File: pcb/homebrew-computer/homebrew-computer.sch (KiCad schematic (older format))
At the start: 4 parts

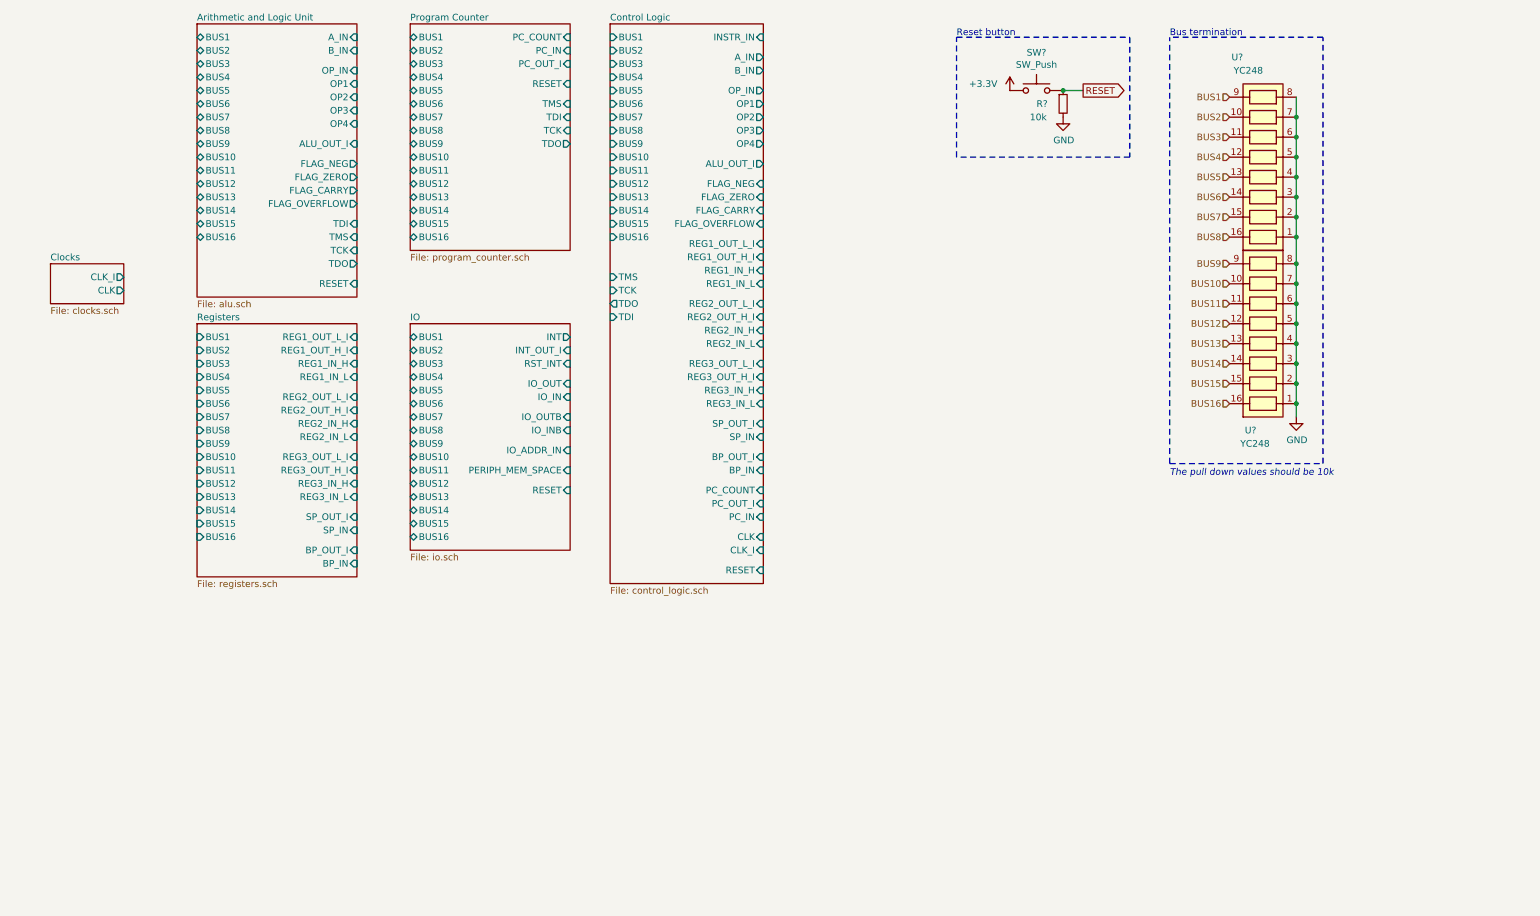
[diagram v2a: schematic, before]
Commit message: Connect signals between modules
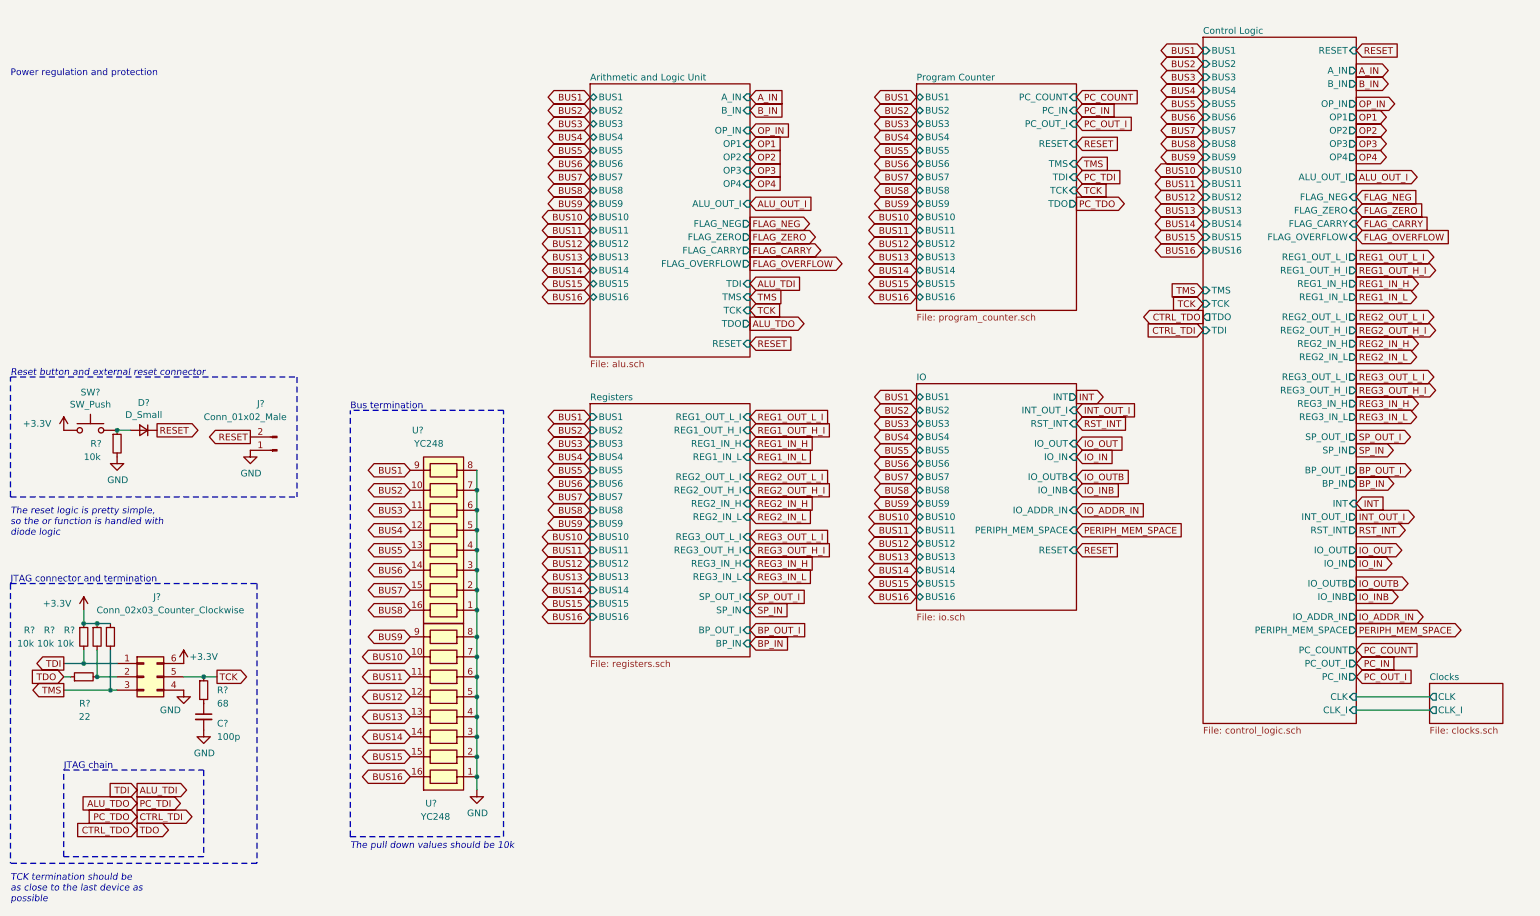
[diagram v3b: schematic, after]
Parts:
- added C?: 100p, symbol Device:C_Small
- added D?: D_Small, symbol Device:D_Small
- added J?: Conn_02x03_Counter_Clockwise, symbol Connector_Generic:Conn_02x03_Counter_Clockwise
- added J?: Conn_01x02_Male, symbol Connector:Conn_01x02_Male
- added R? (x3): 10k, symbol Device:R_Small
- added R?: 68, symbol Device:R_Small
- added R?: 22, symbol Device:R_Small
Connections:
- net +3V3: now also J?.6 (Pin_6), R?.1, R?.1, R?.1
- net GND: now also C?.2, J?.1 (Pin_1), J?.4 (Pin_4)
- net RESET: now also D?.1 (K), J?.2 (Pin_2); no longer R?.1, SW?.2
- new net: J?.2 (Pin_2), R?.2, R?.2
- new net: C?.1, R?.2
- new net: D?.2 (A), R?.1, SW?.2
- new net ALU_TDI: J?.1 (Pin_1), R?.2
- new net CTRL_TDO: R?.1
- new net TCK: J?.5 (Pin_5), R?.1
- new net TMS: J?.3 (Pin_3), R?.2
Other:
- note added: "JTAG chain"
- note added: "JTAG connector and termination"
- note added: "Power regulation and protection"
- note added: "Reset button and external reset connector"
- note added: "TCK termination should be \nas close to the last device as\npossible"
- note added: "The reset logic is pretty simple, \nso the or function is handled with\ndiode logic"
- note removed: "Reset button"
- moved on the sheet: R?, SW?, U?

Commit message: Start changing global labels with local labels
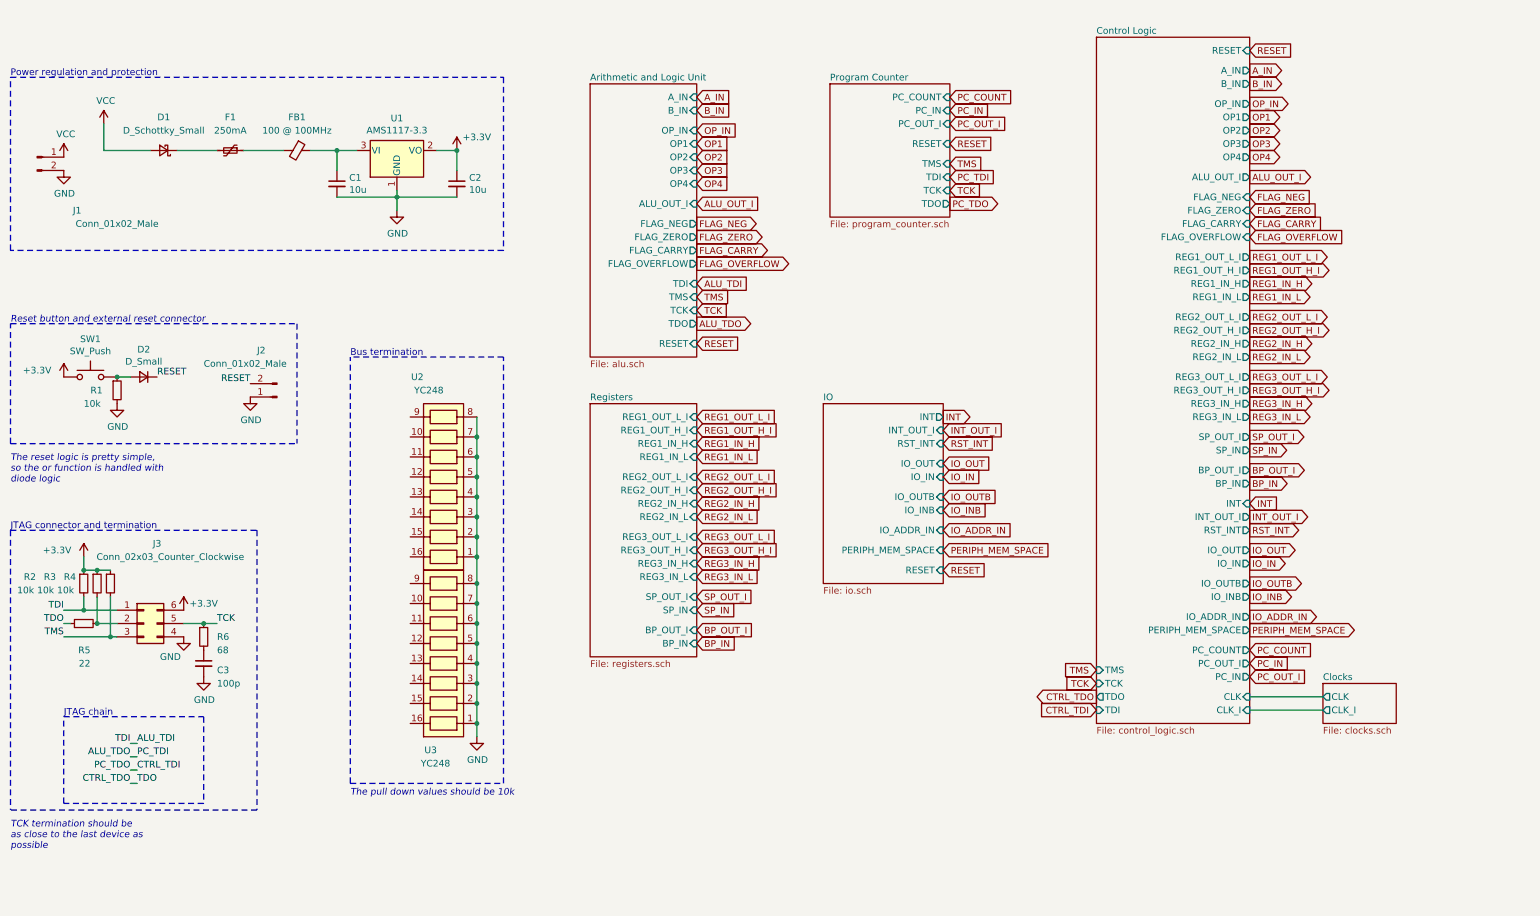
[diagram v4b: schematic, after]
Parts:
- added C1, C2: 10u, symbol Device:C_Small
- added D1: D_Schottky_Small, symbol Device:D_Schottky_Small
- added F1: 250mA, symbol Device:Polyfuse_Small
- added FB1: 100 @ 100MHz, symbol Device:Ferrite_Bead_Small
- added J1: Conn_01x02_Male, symbol Connector:Conn_01x02_Male
- added U1: AMS1117-3.3, Package_TO_SOT_SMD:SOT-223-3_TabPin2, symbol Regulator_Linear:AMS1117-3.3
- gave numbers to parts that had none: 13
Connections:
- net +3V3: now also C2.1, U1.2 (VO)
- net GND: now also C1.2, C2.2, J1.2 (Pin_2), U1.1 (GND)
- net BUS1: no longer names the net of U2.9
- net BUS10: no longer names the net of U3.10
- net BUS11: no longer names the net of U3.11
- net BUS12: no longer names the net of U3.12
- net BUS13: no longer names the net of U3.13
- net BUS14: no longer names the net of U3.14
- net BUS15: no longer names the net of U3.15
- net BUS16: no longer names the net of U3.16
- net BUS2: no longer names the net of U2.10
- net BUS3: no longer names the net of U2.11
- net BUS4: no longer names the net of U2.12
- net BUS5: no longer names the net of U2.13
- net BUS6: no longer names the net of U2.14
- net BUS7: no longer names the net of U2.15
- net BUS8: no longer names the net of U2.16
- net BUS9: no longer names the net of U3.9
- new net: F1.1, FB1.2
- new net: D1.1 (K), F1.2
- new net: C1.1, FB1.1, U1.3 (VI)
- new net VCC: D1.2 (A), J1.1 (Pin_1)
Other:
- moved on the sheet: C3, D2, J2, J3, R1, R2, R3, R4, R5, R6, SW1, U2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

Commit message: Start working on the pcb layout
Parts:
- C1, C2: footprint (none) -> Capacitor_SMD:C_0603_1608Metric
- C3: footprint (none) -> Capacitor_SMD:C_0402_1005Metric_Pad0.74x0.62mm_HandSolder
- D1, D2: footprint (none) -> Diode_SMD:D_0603_1608Metric
- F1: footprint (none) -> Fuse:Fuse_1206_3216Metric_Pad1.42x1.75mm_HandSolder
- FB1, R1, R2, R3, R4, R5, R6: footprint (none) -> Resistor_SMD:R_0603_1608Metric
- J1, J2: footprint (none) -> Connector_Molex:Molex_PicoBlade_53048-0210_1x02_P1.25mm_Horizontal
- J3: footprint (none) -> Connector_PinHeader_2.54mm:PinHeader_2x03_P2.54mm_Vertical
- SW1: footprint (none) -> Button_Switch_SMD:Panasonic_EVQPUL_EVQPUC
- U2, U3: footprint (none) -> Resistor_SMD:YC248
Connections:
- net BUS10: now reaches U3.10
- net BUS11: now reaches U3.11
- net BUS12: now reaches U3.12
- net BUS13: now reaches U3.13
- net BUS14: now reaches U3.14
- net BUS15: now reaches U3.15
- net BUS16: now reaches U3.16
- net BUS9: now reaches U3.9
- net BUS2: now reaches U2.10
- net BUS3: now reaches U2.11
- net BUS4: now reaches U2.12
- net BUS5: now reaches U2.13
- net BUS6: now reaches U2.14
- net BUS7: now reaches U2.15
- net BUS8: now reaches U2.16
- net BUS1: now reaches U2.9
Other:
- moved on the sheet: J1

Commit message: Keep working on the layout
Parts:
- J1, J2: footprint Connector_Molex:Molex_PicoBlade_53048-0210_1x02_P1.25mm_Horizontal -> Connector_Molex:Molex_Pico-Clasp_202396-0207_1x02-1MP_P1.00mm_Horizontal
- J3: footprint Connector_PinHeader_2.54mm:PinHeader_2x03_P2.54mm_Vertical -> Connector_Molex:Molex_Pico-Clasp_202396-0607_1x06-1MP_P1.00mm_Horizontal
- R1, R2, R3, R4, R5, R6: footprint Resistor_SMD:R_0603_1608Metric -> Resistor_SMD:R_0402_1005Metric_Pad0.72x0.64mm_HandSolder
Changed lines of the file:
@@
 F 0 "R1" H 1450 3600 50  0000 L CNN
 F 1 "10k" H 1400 3500 50  0000 L CNN
-F 2 "Resistor_SMD:R_0603_1608Metric" H 1650 3600 50  0001 C CNN
+F 2 "Resistor_SMD:R_0402_1005Metric_Pad0.72x0.64mm_HandSolder" H 1650 3600 50  0001 C CNN
 F 3 "~" H 1650 3600 50  0001 C CNN
 	1    1650 3600
@@
 F 0 "R2" H 950 5100 50  0000 L CNN
 F 1 "10k" H 900 5000 50  0000 L CNN
-F 2 "Resistor_SMD:R_0603_1608Metric" H 1400 5050 50  0001 C CNN
+F 2 "Resistor_SMD:R_0402_1005Metric_Pad0.72x0.64mm_HandSolder" H 1400 5050 50  0001 C CNN
 F 3 "~" H 1400 5050 50  0001 C CNN
 	1    1400 5050
@@
 F 0 "R3" H 1100 5100 50  0000 L CNN
 F 1 "10k" H 1050 5000 50  0000 L CNN
-F 2 "Resistor_SMD:R_0603_1608Metric" H 1500 5050 50  0001 C CNN
+F 2 "Resistor_SMD:R_0402_1005Metric_Pad0.72x0.64mm_HandSolder" H 1500 5050 50  0001 C CNN
 F 3 "~" H 1500 5050 50  0001 C CNN
 	1    1500 5050
@@
 F 0 "R4" H 1250 5100 50  0000 L CNN
 F 1 "10k" H 1200 5000 50  0000 L CNN
-F 2 "Resistor_SMD:R_0603_1608Metric" H 1600 5050 50  0001 C CNN
+F 2 "Resistor_SMD:R_0402_1005Metric_Pad0.72x0.64mm_HandSolder" H 1600 5050 50  0001 C CNN
 F 3 "~" H 1600 5050 50  0001 C CNN
 	1    1600 5050
@@
 F 0 "R6" H 2400 5450 50  0000 L CNN
 F 1 "68" H 2400 5350 50  0000 L CNN
-F 2 "Resistor_SMD:R_0603_1608Metric" H 2300 5450 50  0001 C CNN
+F 2 "Resistor_SMD:R_0402_1005Metric_Pad0.72x0.64mm_HandSolder" H 2300 5450 50  0001 C CNN
 F 3 "~" H 2300 5450 50  0001 C CNN
 	1    2300 5450
@@
 F 0 "R5" V 1200 5300 50  0000 L CNN
 F 1 "22" V 1100 5300 50  0000 L CNN
-F 2 "Resistor_SMD:R_0603_1608Metric" H 1400 5350 50  0001 C CNN
+F 2 "Resistor_SMD:R_0402_1005Metric_Pad0.72x0.64mm_HandSolder" H 1400 5350 50  0001 C CNN
 F 3 "~" H 1400 5350 50  0001 C CNN
 	1    1400 5350
@@
 F 0 "J2" H 3000 3300 50  0000 R CNN
 F 1 "Conn_01x02_Male" H 3400 3400 50  0000 R CNN
-F 2 "Connector_Molex:Molex_PicoBlade_53048-0210_1x02_P1.25mm_Horizontal" H 2850 3650 50  0001 C CNN
+F 2 "Connector_Molex:Molex_Pico-Clasp_202396-0207_1x02-1MP_P1.00mm_Horizontal" H 2850 3650 50  0001 C CNN
 F 3 "~" H 2850 3650 50  0001 C CNN
 	1    2850 3650
@@
 F 0 "J1" H 1250 1450 50  0000 C CNN
 F 1 "Conn_01x02_Male" H 1550 1350 50  0000 C CNN
-F 2 "Connector_Molex:Molex_PicoBlade_53048-0210_1x02_P1.25mm_Horizontal" H 950 1850 50  0001 C CNN
+F 2 "Connector_Molex:Molex_Pico-Clasp_202396-0207_1x02-1MP_P1.00mm_Horizontal" H 950 1850 50  0001 C CNN
 F 3 "~" H 950 1850 50  0001 C CNN
 	1    950  1850
@@
 F 0 "J3" H 1950 5950 50  0000 C CNN
 F 1 "Conn_02x03_Counter_Clockwise" H 2050 5850 50  0000 C CNN
-F 2 "Connector_PinHeader_2.54mm:PinHeader_2x03_P2.54mm_Vertical" H 1850 5350 50  0001 C CNN
+F 2 "Connector_Molex:Molex_Pico-Clasp_202396-0607_1x06-1MP_P1.00mm_Horizontal" H 1850 5350 50  0001 C CNN
 F 3 "~" H 1850 5350 50  0001 C CNN
 	1    1850 5350

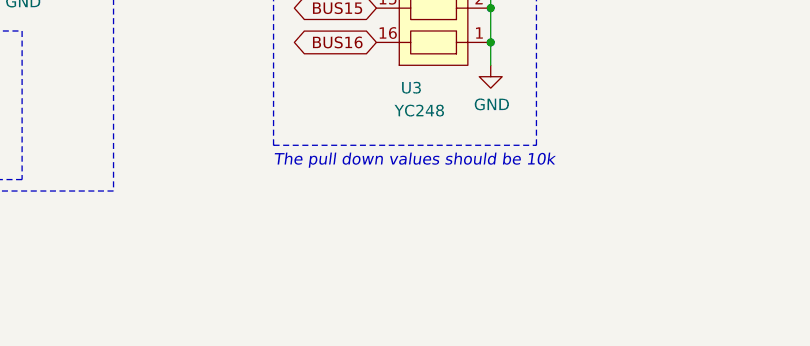
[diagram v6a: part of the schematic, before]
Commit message: Add the board outline
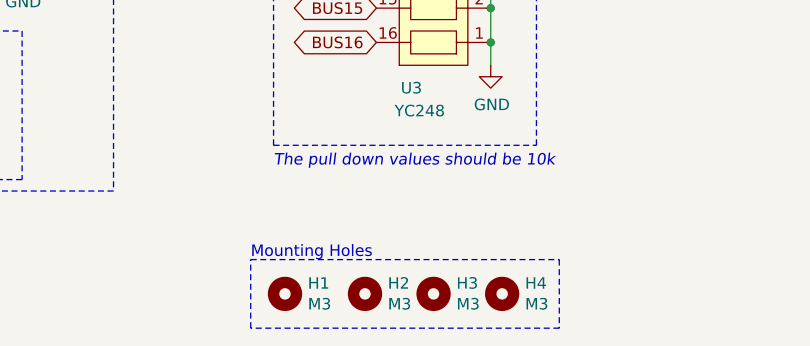
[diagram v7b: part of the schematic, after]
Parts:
- added H1, H2, H3, H4: M3, MountingHole:MountingHole_2.7mm_M2.5, symbol Mechanical:MountingHole
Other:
- note added: "Mounting Holes"
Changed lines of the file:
@@
 	1    0    0    -1
 $EndComp
+$Comp
+L Mechanical:MountingHole H1
+U 1 1 5FA3BEDC
+P 3450 7200
+F 0 "H1" H 3550 7246 50  0000 L CNN
+F 1 "M3" H 3550 7155 50  0000 L CNN
+F 2 "MountingHole:MountingHole_2.7mm_M2.5" H 3450 7200 50  0001 C CNN
+F 3 "~" H 3450 7200 50  0001 C CNN
+	1    3450 7200
+	1    0    0    -1
+$EndComp
+$Comp
+L Mechanical:MountingHole H2
+U 1 1 5FA3C065
+P 3800 7200
+F 0 "H2" H 3900 7246 50  0000 L CNN
+F 1 "M3" H 3900 7155 50  0000 L CNN
+F 2 "MountingHole:MountingHole_2.7mm_M2.5" H 3800 7200 50  0001 C CNN
+F 3 "~" H 3800 7200 50  0001 C CNN
+	1    3800 7200
+	1    0    0    -1
+$EndComp
+$Comp
+L Mechanical:MountingHole H3
+U 1 1 5FA3C31E
+P 4100 7200
+F 0 "H3" H 4200 7246 50  0000 L CNN
+F 1 "M3" H 4200 7155 50  0000 L CNN
+F 2 "MountingHole:MountingHole_2.7mm_M2.5" H 4100 7200 50  0001 C CNN
+F 3 "~" H 4100 7200 50  0001 C CNN
+	1    4100 7200
+	1    0    0    -1
+$EndComp
+$Comp
+L Mechanical:MountingHole H4
+U 1 1 5FA3C4FA
+P 4400 7200
+F 0 "H4" H 4500 7246 50  0000 L CNN
+F 1 "M3" H 4500 7155 50  0000 L CNN
+F 2 "MountingHole:MountingHole_2.7mm_M2.5" H 4400 7200 50  0001 C CNN
+F 3 "~" H 4400 7200 50  0001 C CNN
+	1    4400 7200
+	1    0    0    -1
+$EndComp
+Wire Notes Line
+	3300 7050 4650 7050
+Wire Notes Line
+	4650 7050 4650 7350
+Wire Notes Line
+	4650 7350 3300 7350
+Wire Notes Line
+	3300 7350 3300 7050
+Text Notes 3300 7050 0    50   ~ 0
+Mounting Holes
 $EndSCHEMATC
